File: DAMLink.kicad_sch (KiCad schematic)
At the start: 70 parts, among them J3 USB_C_Receptacle_Host, J4 ARM_JTAG_SWD_10_Male, J4 VCCIO_EXT, J5 PicoBlade, P1 USB_C_Plug, SW1 SW_DIP_x04, U1 FT230XQ, U2 PI5A3157CEX, U3 PI5A3157CEX, U4 USB3740B-AI2, U5 SiP32432DR3, U6 USBLC6-4SC6, U7 USBLC6-4SC6

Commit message: Add new analog switch
Add new analog switch which has more ports to switch between SWD interface and a debug interface.
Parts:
- added U8: TS3A27518EPW, Package_SO:TSSOP-24_4.4x7.8mm_P0.65mm, symbol Analog_Switch:TS3A27518EPW
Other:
- moved on the sheet: C1, C5, C6, D1, D2, J4, J5, JP1, JP2, JP5, JP6, JP7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

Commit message: Update DAMLink.kicad_sch
Removed FTDI Chip, add stlink connector which uses vcp_usart
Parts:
- removed C1: 100nF, Capacitor_SMD:C_0603_1608Metric, symbol Device:C
- removed D1: TXD, LED_SMD:LED_0603_1608Metric, symbol Device:LED
- removed D2: RXD, LED_SMD:LED_0603_1608Metric, symbol Device:LED
- removed J4: ARM_JTAG_SWD_10_Male, tuna-f1sh/jbr-kicad/Misc.pretty:20021521-00010T1LF, symbol Connector:Conn_ARM_JTAG_SWD_10
- removed J5: PicoBlade, Connector_PinHeader_1.27mm:PinHeader_1x04_P1.27mm_Vertical, symbol minnow-rescue:Conn_01x04_Male-Connector
- removed JP7: SolderJumper_2_Bridged, Jumper:SolderJumper-2_P1.3mm_Bridged_RoundedPad1.0x1.5mm, symbol Jumper:SolderJumper_2_Bridged
- removed R1, R2: 1k, Resistor_SMD:R_0603_1608Metric, symbol Device:R_Small
- removed R15, R7, R8, R9: 680R, Resistor_SMD:R_0603_1608Metric, symbol Device:R_Small
- removed TP5, TP6: TestPoint_Small, tuna-f1sh/jbr-kicad/Misc.pretty:TestPoint_Pad_D1.0mm_Tight, symbol Connector:TestPoint_Small
- removed U1: FT230XQ, Package_DFN_QFN:QFN-16-1EP_4x4mm_P0.65mm_EP2.1x2.1mm, symbol Interface_USB:FT230XQ
- removed U8: TS3A27518EPW, Package_SO:TSSOP-24_4.4x7.8mm_P0.65mm, symbol Analog_Switch:TS3A27518EPW
- added C7, C8: 100nF, symbol Device:C
- added J2: Conn_ST_STDC14, symbol Connector:Conn_ST_STDC14
- added JP8, JP9: SolderJumper_2_Bridged, Jumper:SolderJumper-2_P1.3mm_Bridged_RoundedPad1.0x1.5mm, symbol Jumper:SolderJumper_2_Bridged
- added R17, R18: 22k, Resistor_SMD:R_0603_1608Metric, symbol Device:R_Small
- added U8, U9: NC7SB3157L6X, Package_SON:Fairchild_MicroPak-6_1.0x1.45mm_P0.5mm, symbol Analog_Switch:NC7SB3157L6X
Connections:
- net DEV_RXD: now also JP8.1 (A)
- net DEV_TXD: now also JP9.1 (A)
- net GND: now also C7.2, C8.2, J2.11 (GNDDetect), J2.5 (GND), J2.7 (GND), R17.2, R18.2, U8.2 (GND), U9.2 (GND)
- net SWCLK: now also J2.6 (JCLK/SWCLK), U8.3; no longer P1.B3 (TX2-)
- net SWDIO: now also J2.4 (JTMS/SWDIO), U9.3; no longer P1.B2 (TX2+)
- net SWO: now also J2.8 (JTDO/SWO)
- net SWT_RX-: now also R17.1, R18.1, U8.6, U9.6
- net VREF: now also J2.3 (VCC)
- net ~{RESET}: now also J2.12 (~{RST})
- net TXDEN/CB0 renamed DEV_TX-
- net DEV_TX-: now also U8.4
- net TXLED/CB1 renamed DEV_TX+
- net DEV_TX+: now also U9.4
- new net: C8.1, U9.5 (V+)
- new net: J2.13 (VCP_RX), JP8.2 (B)
- new net: J2.14 (VCP_TX), JP9.2 (B)
- new net: C7.1, U8.5 (V+)
- no-connect marks 13 -> 12
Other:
- note removed: "Default sleep is active low so will turn off device with power! Configure as GPIO or PWREN# for VBUS control"
- note removed: "Lahels are default use for CBUS but can be configured/scripted. All to VCCIO so require VCC; cannot use to switch DEV_ON without JP5 linked to 3V3/VEXT. PASS_USB Vh is 1.4 even though VBUS powered, will also disconnect UART!"
- note removed: "Provides USB UART interface to device when RXD/TXD on USB-RX pins"
- moved on the sheet: C5, C6, JP1, JP2, R5, R6, TP17, TP18, U2A, U2B, U3A, U3B

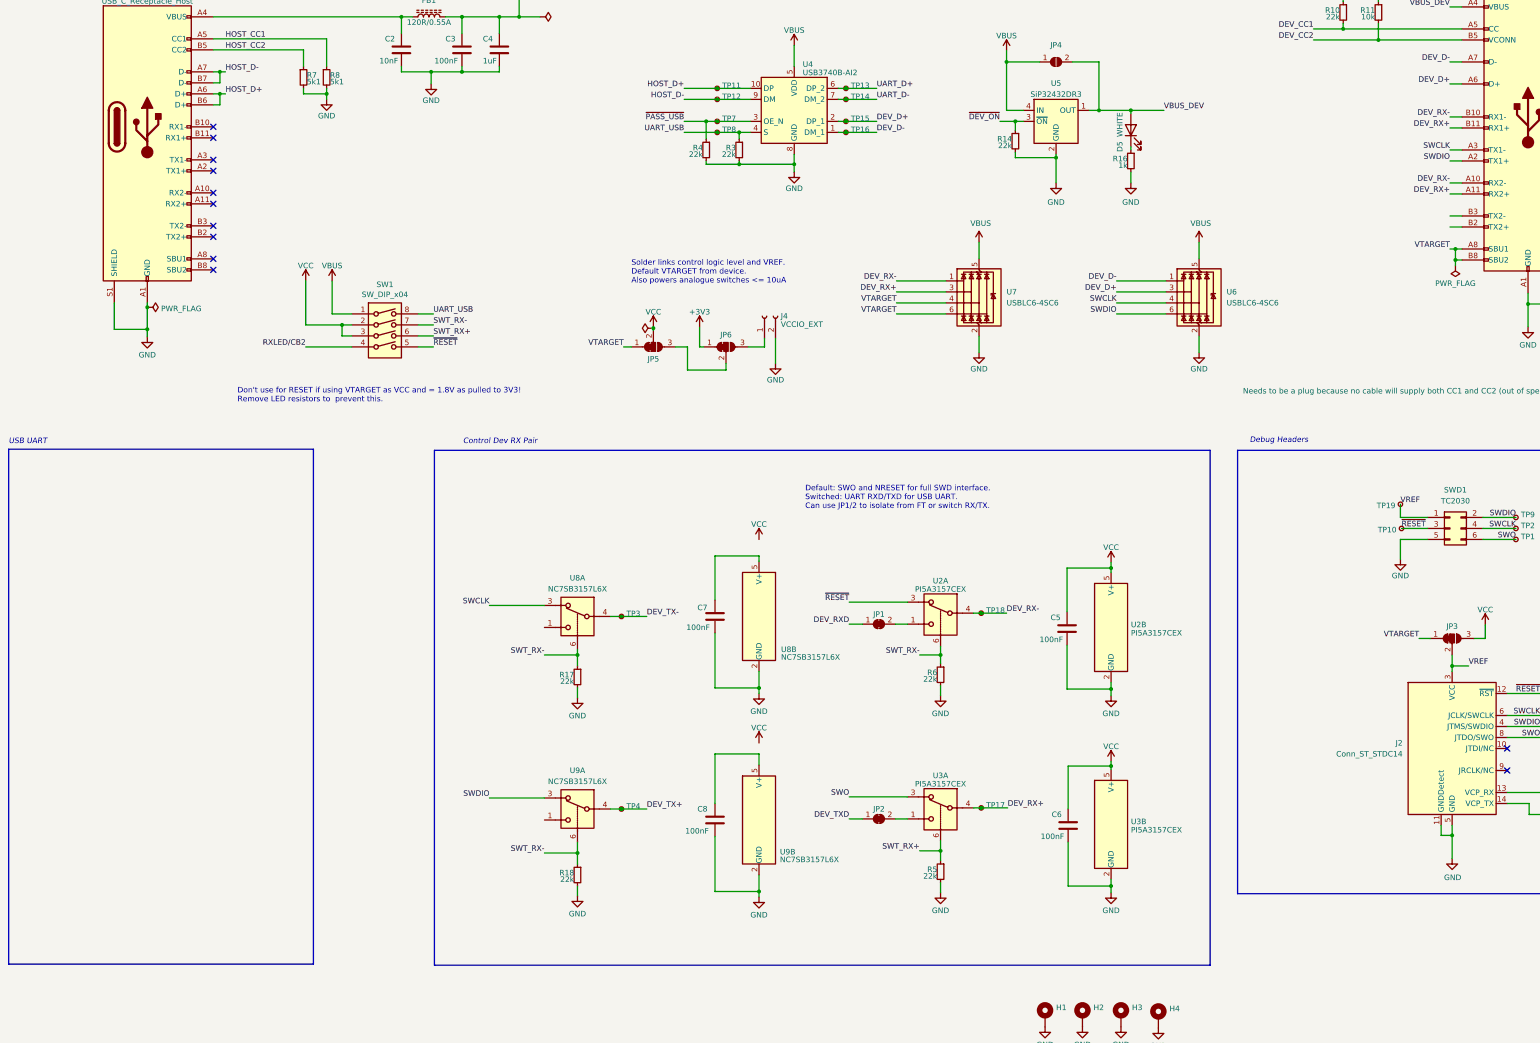
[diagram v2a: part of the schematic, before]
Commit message: Update DAMLink.kicad_sch
working on schematics
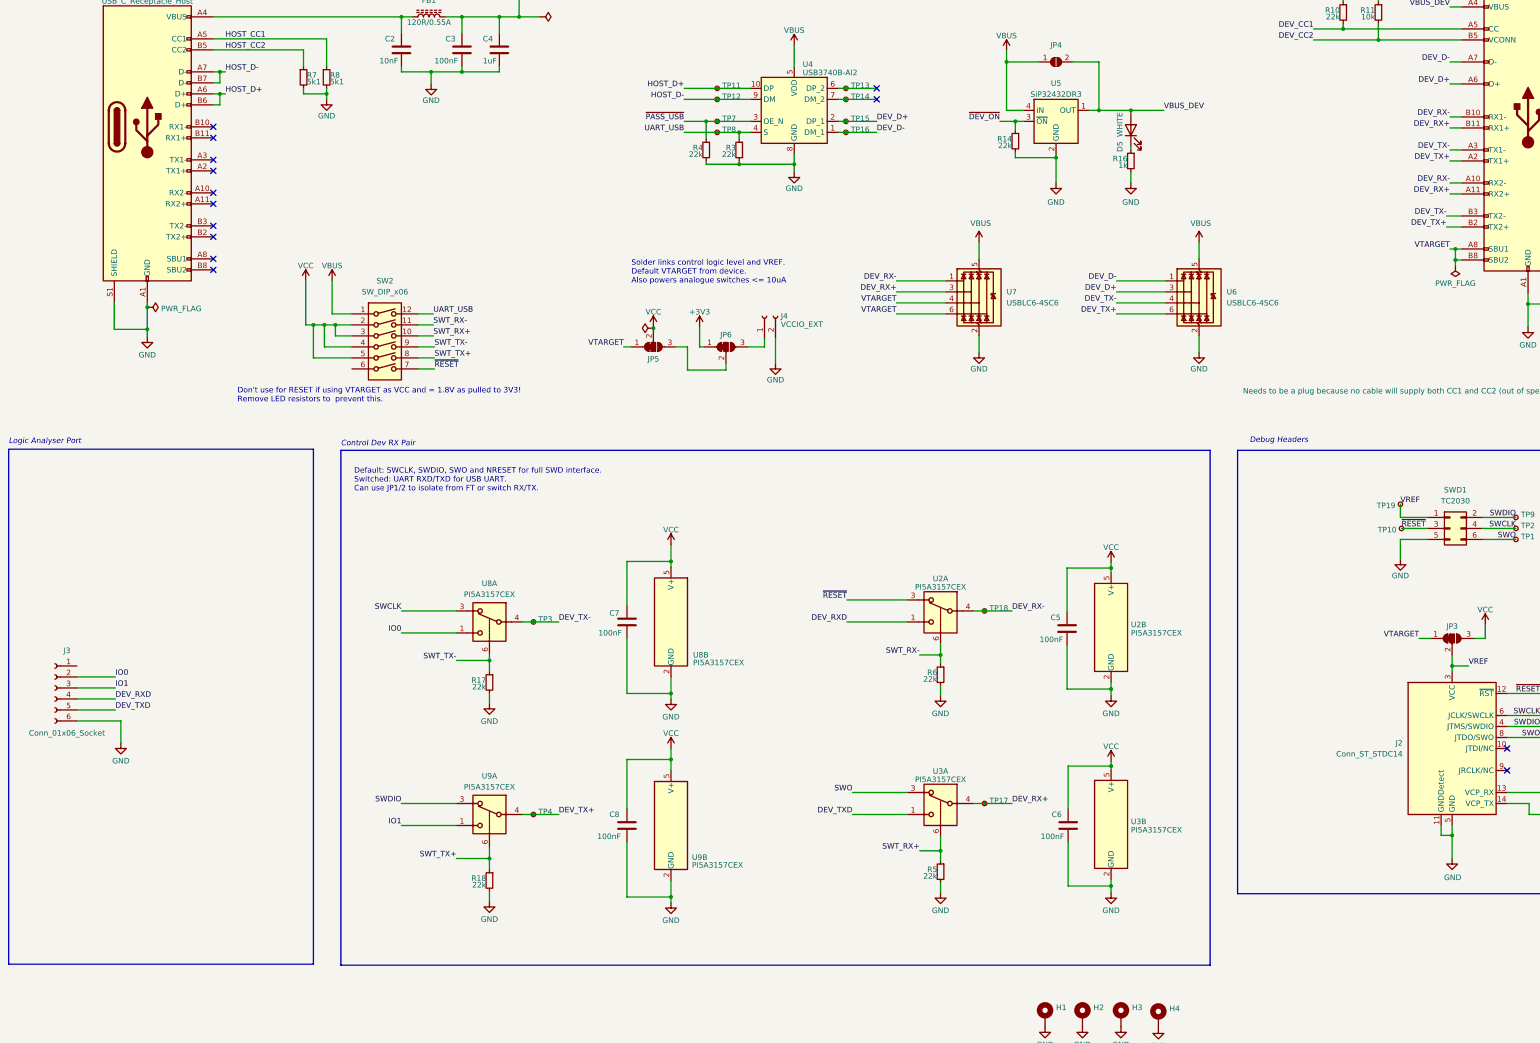
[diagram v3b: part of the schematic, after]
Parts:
- removed JP1, JP2: SolderJumper_2_Bridged, Jumper:SolderJumper-2_P1.3mm_Bridged_RoundedPad1.0x1.5mm, symbol Jumper:SolderJumper_2_Bridged
- removed SW1: SW_DIP_x04, Button_Switch_SMD:SW_DIP_SPSTx04_Slide_Copal_CHS-04A_W5.08mm_P1.27mm_JPin, symbol Switch:SW_DIP_x04
- added J3: Conn_01x06_Socket, symbol Connector:Conn_01x06_Socket
- added SW2: SW_DIP_x06, symbol Switch:SW_DIP_x06
- U8, U9: value NC7SB3157L6X -> PI5A3157CEX
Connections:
- net DEV_RXD: now also U2.1, J3.4 (Pin_4)
- net DEV_TX+: now also P1.A2 (TX1+), P1.B2 (TX2+), U6.6 (I/O4)
- net DEV_TX-: now also P1.A3 (TX1-), P1.B3 (TX2-), U6.4 (I/O3)
- net DEV_TXD: now also U3.1, J3.5 (Pin_5)
- net GND: now also J3.6 (Pin_6)
- net SWCLK: no longer P1.A3 (TX1-), U6.4 (I/O3)
- net SWDIO: no longer P1.A2 (TX1+), U6.6 (I/O4)
- net SWT_RX+: now also SW2.10
- net SWT_RX-: now also SW2.11; no longer R17.1, R18.1, U8.6, U9.6
- net UART_USB: now also SW2.12
- net VBUS: now also SW2.1
- net VCC: now also C7.1, C8.1, U8.5 (V+), U9.5 (V+), SW2.2, SW2.3, SW2.4, SW2.5
- net ~{RESET}: now also SW2.7
- net IO0: now reaches U8.1
- net IO0: now also J3.2 (Pin_2)
- net IO1: now reaches U9.1
- net IO1: now also J3.3 (Pin_3)
- net UART_D+: no longer names the net of TP13.1, U4.6 (DP_2)
- net UART_D-: no longer names the net of TP14.1, U4.7 (DM_2)
- new net SWT_TX+: R18.1, SW2.8, U9.6
- new net SWT_TX-: R17.1, SW2.9, U8.6
- no-connect marks 12 -> 14
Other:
- note added: "Default: SWCLK, SWDIO, SWO and NRESET for full SWD interface. Switched: UART RXD/TXD for USB UART. Can use JP1/2 to isolate from FT or switch RX/TX."
- note added: "Logic Analyser Port"
- note removed: "Default: SWO and NRESET for full SWD interface. Switched: UART RXD/TXD for USB UART. Can use JP1/2 to isolate from FT or switch RX/TX."
- note removed: "USB UART"
- moved on the sheet: C7, C8, R17, R18, TP17, TP18, TP3, TP4, U2A, U3A, U8A, U8B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

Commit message: Update DAMLink.kicad_sch
Changed sheet size to A2
Add FTDI chip back on, since it has some nice features
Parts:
- added C1: 100nF, Capacitor_SMD:C_0603_1608Metric, symbol Device:C
- added D1: TXD, LED_SMD:LED_0603_1608Metric, symbol Device:LED
- added D2: RXD, LED_SMD:LED_0603_1608Metric, symbol Device:LED
- added J5: PicoBlade, Connector_PinHeader_1.27mm:PinHeader_1x04_P1.27mm_Vertical, symbol minnow-rescue:Conn_01x04_Male-Connector
- added JP1: SolderJumper_2_Bridged, Jumper:SolderJumper-2_P1.3mm_Bridged_RoundedPad1.0x1.5mm, symbol Jumper:SolderJumper_2_Bridged
- added R1, R2: 1k, Resistor_SMD:R_0603_1608Metric, symbol Device:R_Small
- added R15, R7, R8, R9: 680R, Resistor_SMD:R_0603_1608Metric, symbol Device:R_Small
- added TP20, TP21, TP5, TP6: TestPoint_Small, tuna-f1sh/jbr-kicad/Misc.pretty:TestPoint_Pad_D1.0mm_Tight, symbol Connector:TestPoint_Small
- added U1: FT230XQ, Package_DFN_QFN:QFN-16-1EP_4x4mm_P0.65mm_EP2.1x2.1mm, symbol Interface_USB:FT230XQ
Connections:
- net +3V3: now also C1.1, D1.2 (A), D2.2 (A), U1.8 (3V3OUT), U1.9 (~{RESET})
- net DEV_RXD: now also J5.3 (Pin_3), U1.2 (RXD)
- net DEV_TXD: now also J5.2 (Pin_2), U1.15 (TXD)
- net GND: now also C1.2, J5.4 (Pin_4), U1.13 (GND), U1.17 (GND), U1.3 (GND)
- net HOST_D+: now also TP7.1; no longer TP11.1
- net HOST_D-: now also TP8.1; no longer TP12.1
- net SWT_RX+: now also R7.2
- net SWT_RX-: now also R8.2
- net UART_USB: now also R4.1, TP12.1; no longer R3.1, TP8.1
- net VBUS: now also JP1.2 (B)
- net VCC: now also J5.1 (Pin_1), U1.1 (VCCIO)
- net ~{DEV_ON}: now also R15.2
- net ~{PASS_USB}: now also R3.1, TP11.1, R9.2; no longer R4.1, TP7.1
- net UART_D-: now reaches TP14.1, U4.7 (DM_2)
- net UART_D-: now also U1.7 (USBDM)
- net RXLED/CB2: now reaches SW2.6
- net RXLED/CB2: now also R2.2, R9.1, TP20.1, U1.5 (CBUS2)
- net UART_D+: now reaches TP13.1, U4.6 (DP_2)
- net UART_D+: now also U1.6 (USBDP)
- new net: D2.1 (K), R2.1
- new net: D1.1 (K), R1.1
- new net: JP1.1 (A), U1.10 (VCC)
- new net SLEEP/CB3: R15.1, TP21.1, U1.14 (CBUS3)
- new net TXDEN/CB0: R7.1, TP5.1, U1.12 (CBUS0)
- new net TXLED/CB1: R1.2, R8.1, TP6.1, U1.11 (CBUS1)
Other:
- note added: "Default sleep is active low so will turn off device with power! Configure as GPIO or PWREN# for VBUS control"
- note added: "ESD protection for device side USB C connector"
- note added: "Lahels are default use for CBUS but can be configured/scripted. All to VCCIO so require VCC; cannot use to switch DEV_ON without JP5 linked to 3V3/VEXT. PASS_USB Vh is 1.4 even though VBUS powered, will also disconnect UART!"
- note added: "Load switch to power target device Short JP4 to always power device"
- note added: "Provides USB UART interface to device when RXD/TXD on USB-RX pins"
- note added: "USB UART"
- note added: "When all DAM pins are switched The signals from the taget can be checkt with a logic analyzer Providing a debug port when developing accessories with e.x. SPI interface"
- moved on the sheet: C5, C6, C7, C8, D5, J2, J3, J4, JP3, JP4, JP5, JP6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

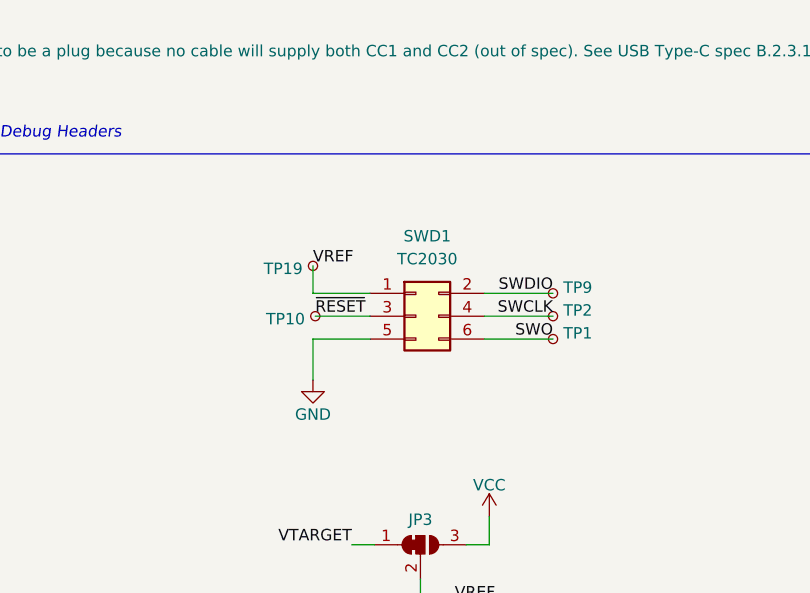
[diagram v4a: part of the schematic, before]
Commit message: Update DAMLink.kicad_sch
Add TC2050 Debug probe (with clips)
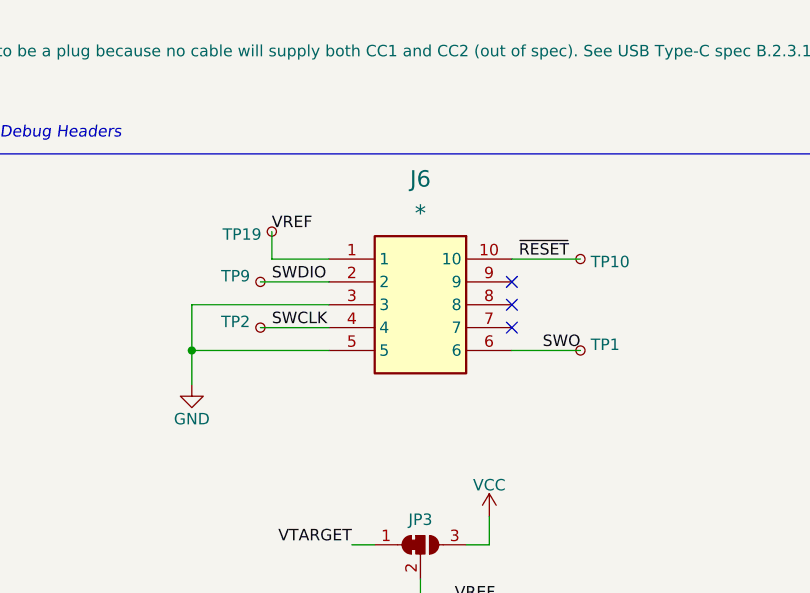
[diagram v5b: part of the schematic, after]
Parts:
- removed SWD1: TC2030, Connector:Tag-Connect_TC2030-IDC-FP_2x03_P1.27mm_Vertical, symbol Connector_Generic:Conn_02x03_Odd_Even
- added J6: *, TC2050-IDC:TAG-CONNECT_TC2050-IDC, symbol TC2050-IDC:TC2050-IDC
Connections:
- net GND: now also J6.3, J6.5
- net SWCLK: now also J6.4
- net SWDIO: now also J6.2
- net SWO: now also J6.6
- net VREF: now also J6.1
- net ~{RESET}: now also J6.10
- no-connect marks 14 -> 17
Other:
- moved on the sheet: TP1, TP10, TP19, TP2, TP9

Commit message: Add new stuff
Add TMUX1574 MUX
Add TC2050 Footprint
Add STDC14 Footprint
Removed PI5A3157 MUX

Now full swd port can be switched with test port
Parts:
- removed C6: 100nF, Capacitor_SMD:C_0603_1608Metric, symbol Device:C
- removed C7, C8: 100nF, symbol Device:C
- removed R17, R18, R5, R6: 22k, Resistor_SMD:R_0603_1608Metric, symbol Device:R_Small
- removed SW2: SW_DIP_x06, symbol Switch:SW_DIP_x06
- removed TP17, TP18, TP3, TP4: TestPoint_Small, tuna-f1sh/jbr-kicad/Misc.pretty:TestPoint_Pad_D1.0mm_Tight, symbol Connector:TestPoint_Small
- removed U2, U3: PI5A3157CEX, Package_TO_SOT_SMD:SOT-363_SC-70-6, symbol Analog_Switch:NC7SB3157P6X
- removed U8, U9: PI5A3157CEX, Package_SON:Fairchild_MicroPak-6_1.0x1.45mm_P0.5mm, symbol Analog_Switch:NC7SB3157L6X
- added SW1: SW_DIP_x04, Button_Switch_SMD:SW_DIP_SPSTx04_Slide_Copal_CHS-04A_W5.08mm_P1.27mm_JPin, symbol Switch:SW_DIP_x04
- added U3: TMUX1574RSVR, TMUX1574RSVR:IC_TMUX1574RSVR, symbol TMUX1574RSVR:TMUX1574RSVR
- J1: renamed from J3; footprint (none) -> Connector_Molex:Molex_PicoBlade_53048-0610_1x06_P1.25mm_Horizontal
- J5: renamed from J6; value * -> TC2050-IDC
- J6: renamed from J2; footprint (none) -> Connector_STDC14:SAMTEC_FTSH-107-01-L-DV-K-A
- renumbered C2 to C1, C3 to C2, C1 to C3, J5 to J3, JP5 to JP2, JP6 to JP3, JP3 to JP5, JP8 to JP6, JP9 to JP7, R15 to R10, R14 to R11, R16 to R12, R10 to R13, R11 to R14, R1 to R5, R2 to R6, TP7 to TP1, TP14 to TP10, TP15 to TP11, TP16 to TP12, TP9 to TP13, TP2 to TP14, TP19 to TP15, TP10 to TP16, TP1 to TP17, TP8 to TP2, TP11 to TP3, TP12 to TP4, TP20 to TP7, TP21 to TP8, TP13 to TP9, U4 to U2, U7 to U4
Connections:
- net DEV_RX+: now also U3.10 (D4)
- net DEV_RX-: now also U3.7 (D3)
- net DEV_RXD: now also U3.8 (S3B)
- net DEV_TX+: now also U3.5 (D2)
- net DEV_TX-: now also U3.2 (D1)
- net DEV_TXD: now also U3.11 (S4B)
- net GND: now also U3.6 (GND)
- net IO0: now also U3.1 (S1B)
- net IO1: now also U3.4 (S2B)
- net RXLED/CB2: now also SW1.4
- net SWCLK: now also U3.16 (S1A)
- net SWDIO: now also U3.3 (S2A)
- net SWO: now also U3.12 (S4A)
- net SWT_RX+: now also SW1.6, U3.15 (SEL)
- net SWT_RX-: now also SW1.7, U3.13 (~{EN})
- net UART_USB: now also SW1.8
- net VBUS: now also SW1.1
- net VCC: now also J1.1 (Pin_1), SW1.2, SW1.3, U3.14 (VDD)
- net ~{RESET}: now also SW1.5, U3.9 (S3A)
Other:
- note added: "Mounting holes tied to gnd"
- note added: "Option 1: TC2050 debugging probe, flash and debug using full SWD Option 2: STDC14 connector, flash, debugging with additional USART interface"
- note added: "TMUX1574 Low-Capacitance, 2:1 (SPDT) 4-Channel SW_RX-: High disable chip / Low enables chip SW_RX+: High connect PORT B to output (D1-D4) / Low connect PORT A to output Default: Full SWD is switched to device port"
- note added: "~{EN} Pin: Active low enable: When this pin is high, all switches are turned off. When this pin is low, SEL pin controls the signal path selection. Internal 6 MΩ pull-down to GND SEL Pin: Select pin: controls state of switches according to Table 1. Internal 6 MΩ pull-down to GND"
- note removed: "Default: SWCLK, SWDIO, SWO and NRESET for full SWD interface. Switched: UART RXD/TXD for USB UART. Can use JP1/2 to isolate from FT or switch RX/TX."
- moved on the sheet: D5, H1, H2, H3, H4, JP4, R11, R12, U4, U5, U6

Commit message: Add new footprint
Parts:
- added JP8, JP9: SolderJumper_2_Bridged, Jumper:SolderJumper-2_P1.3mm_Bridged_RoundedPad1.0x1.5mm, symbol Jumper:SolderJumper_2_Bridged
- J1: value Conn_01x06_Socket -> PicoBlade
- J6: footprint Connector_STDC14:SAMTEC_FTSH-107-01-L-DV-K-A -> Connector_STDC14:CON14_2X7_DUK_FTSH_SAI
- TP1, TP10, TP11, TP12, TP13, TP14, TP15, TP16, TP17, TP2, TP3, TP4, TP5, TP6, TP7, TP8, TP9: footprint tuna-f1sh/jbr-kicad/Misc.pretty:TestPoint_Pad_D1.0mm_Tight -> TestPoint:TestPoint_Pad_D1.0mm
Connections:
- net DEV_RXD: now also JP9.2 (B); no longer U1.2 (RXD)
- net DEV_TXD: now also JP8.2 (B); no longer U1.15 (TXD)
- net GND: now also J6.05 (GND), J6.07 (GND); no longer J6.5 (GND), J6.7 (GND)
- net SWCLK: now also J6.06 (JCLK/SWCLK); no longer J6.6 (JCLK/SWCLK)
- net SWDIO: now also J6.04 (JTMS/SWDIO); no longer J6.4 (JTMS/SWDIO)
- net SWO: now also J6.08 (JTDO/SWO); no longer J6.8 (JTDO/SWO)
- net VREF: now also J6.03 (VCC); no longer J6.3 (VCC)
- new net: JP8.1 (A), U1.15 (TXD)
- new net: JP9.1 (A), U1.2 (RXD)
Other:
- moved on the sheet: D1, D2, R10, R5, R6, R7, R8, R9
